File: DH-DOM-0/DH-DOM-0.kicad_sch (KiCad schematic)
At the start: 40 parts, among them J1 USB_C_Receptacle_USB2.0_14P, J2 Conn_01x02, SW1 RST, SW2 BOOT, U3 LSM6DSOXTR, U4 MMC5983MA, U5 NCP1117-3.3_SOT223, U6 TVS1400DRV, U7 ESP32-S3-WROOM-1-N16R8, U8 TP4057, U9 ST7789

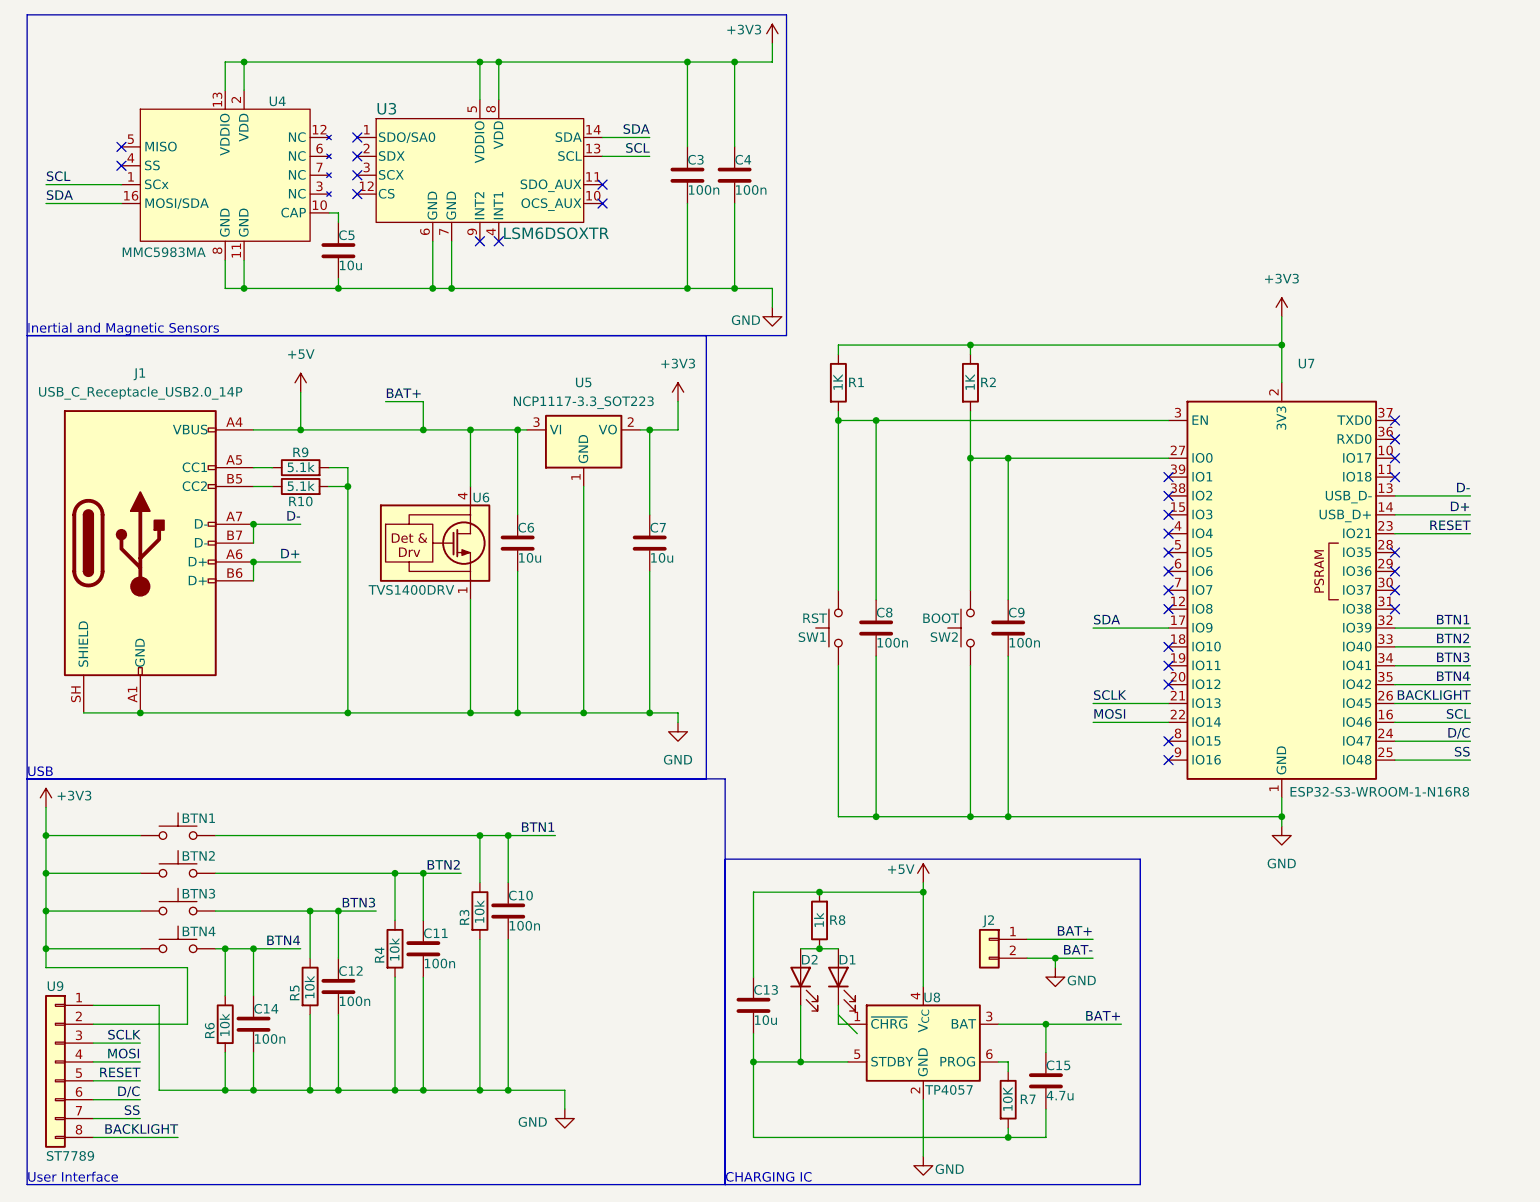
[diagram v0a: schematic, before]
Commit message: edit
battery protection
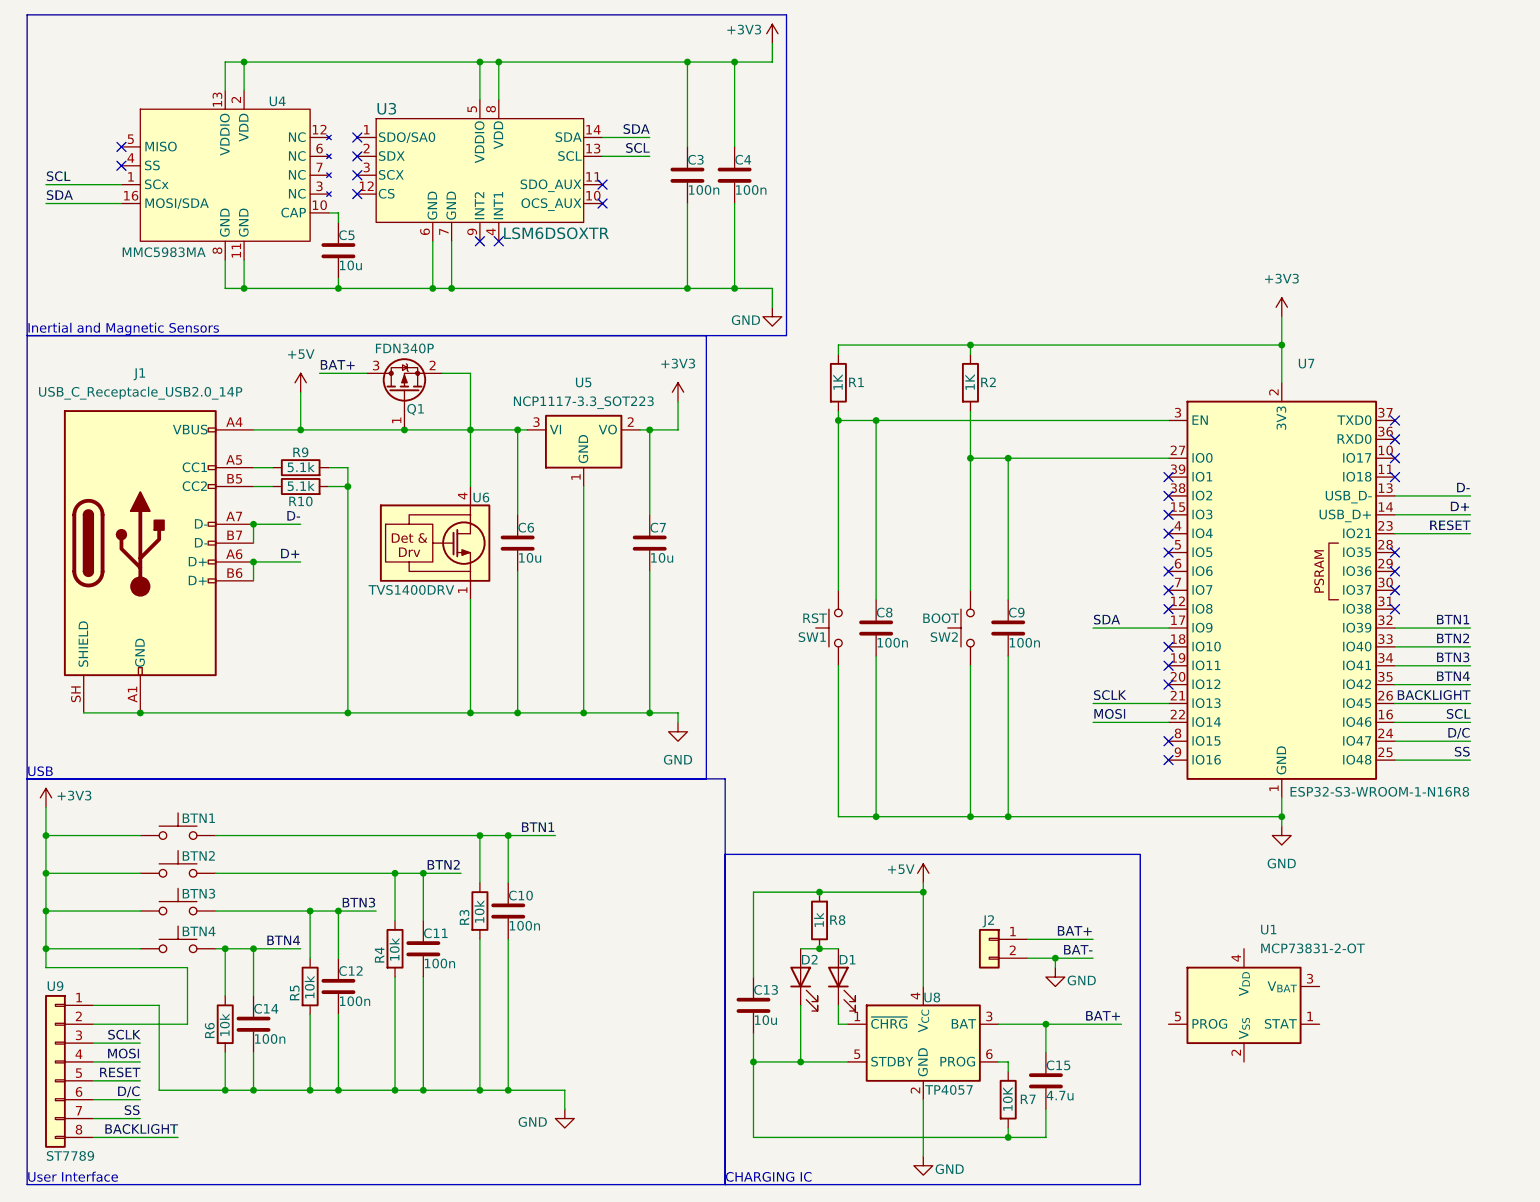
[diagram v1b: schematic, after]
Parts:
- added Q1: FDN340P, Package_TO_SOT_SMD:SOT-23, symbol Transistor_FET:FDN340P
- added U1: MCP73831-2-OT, Package_TO_SOT_SMD:SOT-23-5, symbol Battery_Management:MCP73831-2-OT
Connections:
- net +5V: now also Q1.1 (G), Q1.2 (S); no longer C15.1, J2.1 (Pin_1), U8.3 (BAT)
- new net BAT+: C15.1, J2.1 (Pin_1), Q1.3 (D), U8.3 (BAT)
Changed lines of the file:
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@@
 	(paper "A4")
 	(rectangle
-		(start 106.68 126.365)
+		(start 106.68 125.73)
 		(end 162.56 170.18)
 		(stroke
@@
 	)
 	(junction
-		(at 66.04 68.58)
-		(diameter 0)
-		(color 0 0 0 0)
-	)
-	(junction
 		(at 119.38 138.43)
 		(diameter 0)
@@
 	)
 	(junction
-		(at 43.18 81.28)
+		(at 72.39 68.58)
 		(diameter 0)
 		(color 0 0 0 0)
 	)
 	(junction
-		(at 43.18 138.43)
+		(at 43.18 81.28)
 		(diameter 0)
 		(color 0 0 0 0)
 	)
 	(junction
-		(at 72.39 68.58)
+		(at 43.18 138.43)
 		(diameter 0)
 		(color 0 0 0 0)
@@
 	)
 	(junction
+		(at 63.5 68.58)
+		(diameter 0)
+		(color 0 0 0 0)
+	)
+	(junction
 		(at 39.37 157.48)
 		(diameter 0)
@@
 		(at 196.85 87.63)
 	)
-	(bus_entry
-		(at 121.92 147.32)
-		(size 2.54 2.54)
-		(stroke
-			(width 0)
-			(type default)
-		)
-	)
 	(wire
 		(pts
@@
 	(wire
 		(pts
-			(xy 49.53 68.58) (xy 66.04 68.58)
-		)
-		(stroke
-			(width 0)
-			(type default)
-		)
-	)
-	(wire
-		(pts
 			(xy 38.1 138.43) (xy 39.37 138.43)
 		)
@@
 	(wire
 		(pts
-			(xy 121.92 148.59) (xy 123.19 148.59)
+			(xy 43.18 73.66) (xy 45.72 73.66)
 		)
 		(stroke
@@
 	(wire
 		(pts
-			(xy 43.18 73.66) (xy 45.72 73.66)
+			(xy 15.24 133.35) (xy 27.94 133.35)
 		)
 		(stroke
@@
 	(wire
 		(pts
-			(xy 15.24 133.35) (xy 27.94 133.35)
+			(xy 39.37 49.53) (xy 39.37 45.72)
 		)
 		(stroke
@@
 	(wire
 		(pts
-			(xy 39.37 49.53) (xy 39.37 45.72)
+			(xy 73.66 19.05) (xy 76.2 19.05)
 		)
 		(stroke
@@
 	(wire
 		(pts
-			(xy 73.66 19.05) (xy 76.2 19.05)
+			(xy 68.58 60.96) (xy 72.39 60.96)
 		)
 		(stroke
@@
 	(wire
 		(pts
+			(xy 121.92 148.59) (xy 123.19 148.59)
+		)
+		(stroke
+			(width 0)
+			(type default)
+		)
+	)
+	(wire
+		(pts
 			(xy 15.24 138.43) (xy 27.94 138.43)
 		)
@@
 	(wire
 		(pts
+			(xy 72.39 60.96) (xy 72.39 68.58)
+		)
+		(stroke
+			(width 0)
+			(type default)
+		)
+	)
+	(wire
+		(pts
 			(xy 66.04 128.27) (xy 66.04 134.62)
 		)
@@
 	(wire
 		(pts
-			(xy 60.96 64.77) (xy 66.04 64.77)
-		)
-		(stroke
-			(width 0)
-			(type default)
-		)
-	)
-	(wire
-		(pts
 			(xy 144.78 163.83) (xy 144.78 162.56)
 		)
@@
 	(wire
 		(pts
-			(xy 72.39 68.58) (xy 78.74 68.58)
-		)
-		(stroke
-			(width 0)
-			(type default)
-		)
-	)
-	(wire
-		(pts
 			(xy 15.24 123.19) (xy 15.24 128.27)
 		)
@@
 	(wire
 		(pts
-			(xy 72.39 68.58) (xy 72.39 76.2)
+			(xy 34.29 140.97) (xy 15.24 140.97)
 		)
 		(stroke
@@
 	(wire
 		(pts
-			(xy 34.29 140.97) (xy 15.24 140.97)
+			(xy 116.84 153.67) (xy 123.19 153.67)
 		)
 		(stroke
@@
 	(wire
 		(pts
-			(xy 116.84 153.67) (xy 123.19 153.67)
+			(xy 78.74 80.01) (xy 78.74 68.58)
 		)
 		(stroke
@@
 	(wire
 		(pts
-			(xy 78.74 80.01) (xy 78.74 68.58)
+			(xy 139.7 57.15) (xy 181.61 57.15)
 		)
 		(stroke
@@
 	(wire
 		(pts
-			(xy 139.7 57.15) (xy 181.61 57.15)
+			(xy 50.8 133.35) (xy 50.8 139.7)
 		)
 		(stroke
@@
 	(wire
 		(pts
-			(xy 50.8 133.35) (xy 50.8 139.7)
+			(xy 66.04 128.27) (xy 71.12 128.27)
 		)
 		(stroke
@@
 	(wire
 		(pts
-			(xy 66.04 128.27) (xy 71.12 128.27)
+			(xy 63.5 68.58) (xy 72.39 68.58)
+		)
+		(stroke
+			(width 0)
+			(type default)
+		)
+	)
+	(wire
+		(pts
+			(xy 72.39 68.58) (xy 78.74 68.58)
 		)
 		(stroke
@@
 	(wire
 		(pts
-			(xy 66.04 64.77) (xy 66.04 68.58)
-		)
-		(stroke
-			(width 0)
-			(type default)
-		)
-	)
-	(wire
-		(pts
 			(xy 110.49 153.67) (xy 116.84 153.67)
 		)
@@
 	(wire
 		(pts
-			(xy 66.04 68.58) (xy 72.39 68.58)
+			(xy 49.53 68.58) (xy 63.5 68.58)
 		)
 		(stroke
@@
 	(wire
 		(pts
+			(xy 52.07 60.96) (xy 58.42 60.96)
+		)
+		(stroke
+			(width 0)
+			(type default)
+		)
+	)
+	(wire
+		(pts
 			(xy 34.29 140.97) (xy 34.29 148.59)
 		)
@@
 	(wire
 		(pts
+			(xy 72.39 68.58) (xy 72.39 76.2)
+		)
+		(stroke
+			(width 0)
+			(type default)
+		)
+	)
+	(wire
+		(pts
 			(xy 76.2 19.05) (xy 76.2 24.13)
 		)
@@
 		)
 	)
-	(label "BAT+"
-		(at 60.96 64.77 0)
-		(effects
-			(font
-				(size 1.27 1.27)
-			)
-			(justify left bottom)
-		)
-	)
 	(label "SS"
 		(at 207.01 113.03 180)
@@
 		)
 	)
+	(label "BAT+"
+		(at 52.07 60.96 0)
+		(effects
+			(font
+				(size 1.27 1.27)
+			)
+			(justify left bottom)
+		)
+	)
 	(label "BTN2"
 		(at 71.12 128.27 180)
@@
 	)
 	(symbol
+		(lib_id "Battery_Management:MCP73831-2-OT")
+		(at 176.53 146.05 0)
+		(unit 1)
+		(body_style 1)
+		(exclude_from_sim no)
+		(in_bom yes)
+		(on_board yes)
+		(in_pos_files yes)
+		(dnp no)
+		(fields_autoplaced yes)
+		(property "Reference" "U1"
+			(at 178.6733 135.89 0)
+			(show_name no)
+			(do_not_autoplace no)
+			(effects
+				(font
+					(size 1.27 1.27)
+				)
+				(justify left)
+			)
+		)
+		(property "Value" "MCP73831-2-OT"
+			(at 178.6733 138.43 0)
+			(show_name no)
+			(do_not_autoplace no)
+			(effects
+				(font
+					(size 1.27 1.27)
+				)
+				(justify left)
+			)
+		)
+		(property "Footprint" "Package_TO_SOT_SMD:SOT-23-5"
+			(at 177.8 152.4 0)
+			(hide yes)
+			(show_name no)
+			(do_not_autoplace no)
+			(effects
+				(font
+					(size 1.27 1.27)
+					(italic yes)
+				)
+				(justify left)
+			)
+		)
+		(property "Datasheet" "http://ww1.microchip.com/downloads/en/DeviceDoc/20001984g.pdf"
+			(at 176.53 164.338 0)
+			(hide yes)
+			(show_name no)
+			(do_not_autoplace no)
+			(effects
+				(font
+					(size 1.27 1.27)
+				)
+			)
+		)
+		(property "Description" "Single cell, Li-Ion/Li-Po charge management controller, 4.20V, Tri-State Status Output, in SOT23-5 package"
+			(at 176.53 146.05 0)
+			(hide yes)
+			(show_name no)
+			(do_not_autoplace no)
+			(effects
+				(font
+					(size 1.27 1.27)
+				)
+			)
+		)
+		(pin "2"
+		)
+		(pin "3"
+		)
+		(pin "1"
+		)
+		(pin "5"
+		)
+		(pin "4"
+		)
+		(instances
+			(project "DH-DOM-0"
+				(path "/1a16546f-17ba-458f-9ffb-023bbcd494b0"
+					(reference "U1")
+					(unit 1)
+				)
+			)
+		)
+	)
+	(symbol
 		(lib_id "Device:C")
 		(at 107.95 34.29 0)
@@
 					(unit 1)
 				)
+			)
+		)
+	)
+	(symbol
+		(lib_id "Transistor_FET:FDN340P")
+		(at 63.5 63.5 90)
+		(unit 1)
+		(body_style 1)
+		(exclude_from_sim no)
+		(in_bom yes)
+		(on_board yes)
+		(in_pos_files yes)
+		(dnp no)
+		(property "Reference" "Q1"
+			(at 65.024 65.786 90)
+			(show_name no)
+			(do_not_autoplace no)
+			(effects
+				(font
+					(size 1.27 1.27)
+				)
+			)
+		)
+		(property "Value" "FDN340P"
+			(at 63.5 57.658 90)
+			(show_name no)
+			(do_not_autoplace no)
+			(effects
+				(font
+					(size 1.27 1.27)
+				)
+			)
+		)
+		(property "Footprint" "Package_TO_SOT_SMD:SOT-23"
+			(at 65.405 58.42 0)
+			(hide yes)
+			(show_name no)
+			(do_not_autoplace no)
+			(effects
+				(font
+					(size 1.27 1.27)
+					(italic yes)
+				)
+				(justify left)
+			)
+		)
+		(property "Datasheet" "https://www.onsemi.com/pub/Collateral/FDN340P-D.PDF"
+			(at 67.31 58.42 0)
+			(hide yes)
+			(show_name no)
+			(do_not_autoplace no)
+			(effects
+				(font
+					(size 1.27 1.27)
+				)
+				(justify left)
+			)
+		)
+		(property "Description" "-2A Id, -20V Vds, P-Channel MOSFET, 70mOhm Ron, SOT-23"
+			(at 63.5 63.5 0)
+			(hide yes)
+			(show_name no)
+			(do_not_autoplace no)
+			(effects
+				(font
+					(size 1.27 1.27)
+				)
+			)
+		)
+		(pin "2"
+		)
+		(pin "1"
+		)
+		(pin "3"
+		)
+		(instances
+			(project "DH-DOM-0"
+				(path "/1a16546f-17ba-458f-9ffb-023bbcd494b0"
+					(reference "Q1")
+					(unit 1)
+				)

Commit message: edit
added diode again? idk something happened
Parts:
- removed U1: MCP73831-2-OT, Package_TO_SOT_SMD:SOT-23-5, symbol Battery_Management:MCP73831-2-OT
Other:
- moved on the sheet: C13, C15, C8, C9, D1, D2, J2, Q1, R1, R2, R7, R8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
